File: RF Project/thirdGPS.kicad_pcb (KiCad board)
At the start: 2 copper layers, 30 x 55 mm, 36 parts, among them J1 CONN_Right, J2 CONN_Left, U1 CC2500RGPR, U11 Venus634SMD, U2 U.FL_male, U3 U.FL_male

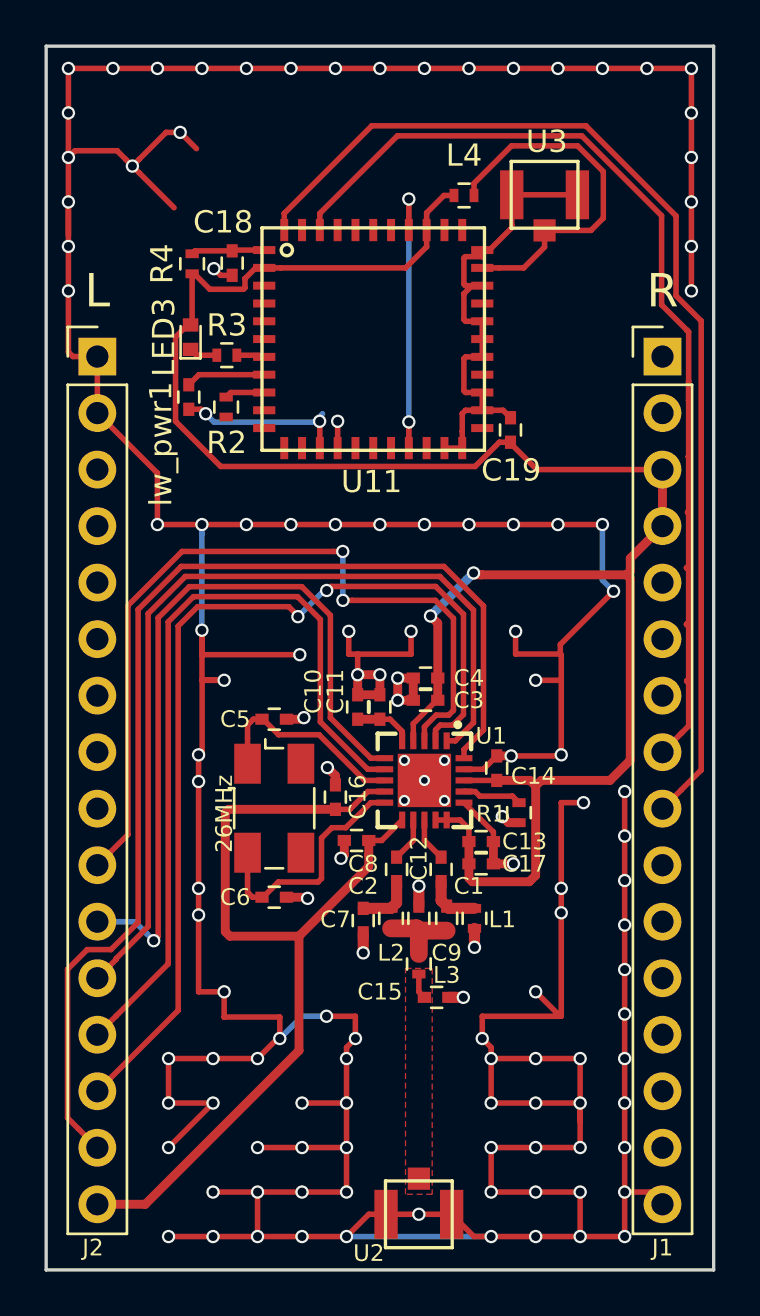
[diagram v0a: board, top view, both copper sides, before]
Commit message: revision component placement, coupling caps added
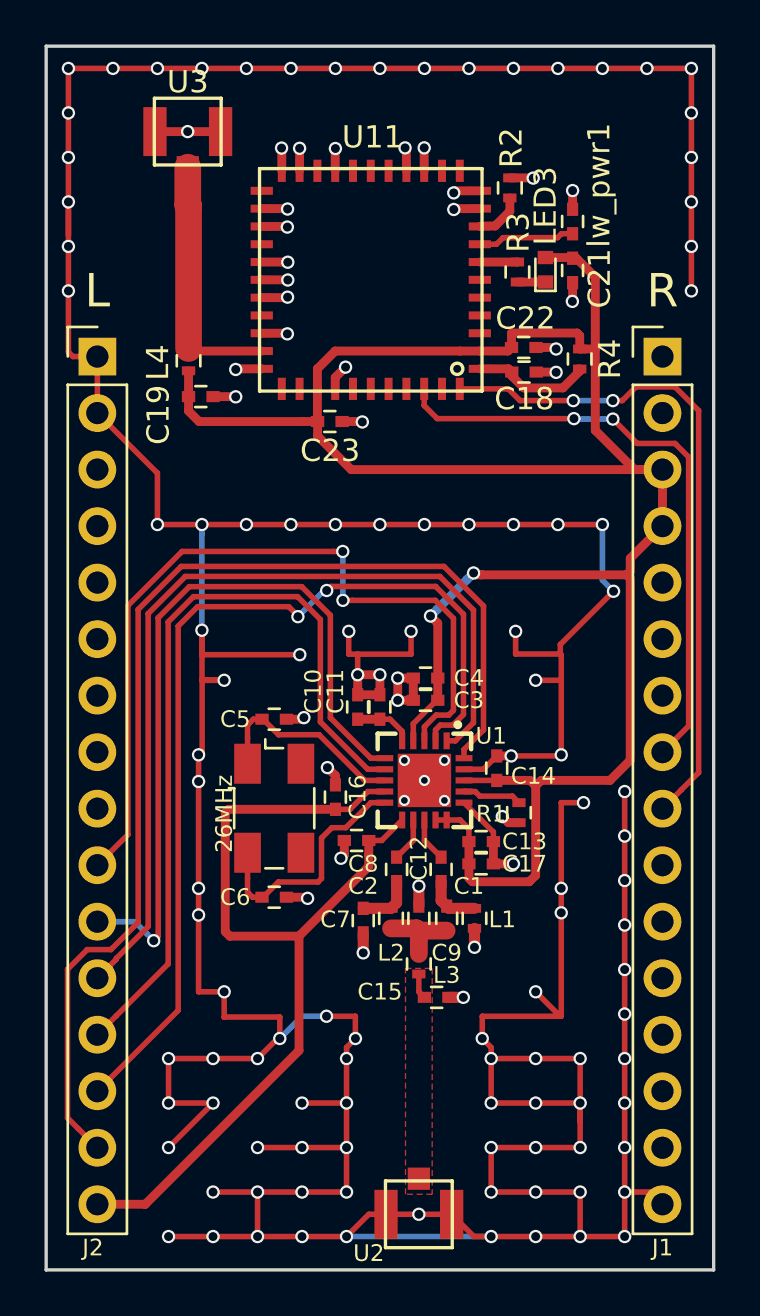
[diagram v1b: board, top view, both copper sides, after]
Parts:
- added C21: 1uF, Capacitors_SMD:C_0402, F.Cu at (108.7, 82.6)
- added C22: 1uF, Capacitors_SMD:C_0402, F.Cu at (106.5, 86.0)
- added C23: 1uF, Capacitors_SMD:C_0402, F.Cu at (97.8, 89.4)
- moved lw_pwr1 19.0 mm to (108.7, 80.4), turned to 90 degrees
- moved R4 17.9 mm to (109.0, 86.6), turned to 270 degrees
- moved U3 16.3 mm to (91.4, 76.3)
- moved LED3 16.2 mm to (107.4, 82.5)
- moved R2 16.1 mm to (105.8, 78.9), turned to 90 degrees
- moved L4 14.4 mm to (91.4, 86.6), turned to 90 degrees
- moved C18 14.0 mm to (106.5, 87.1), turned to 0 degrees
- moved C19 14.0 mm to (92.0, 88.2), turned to 180 degrees
- moved R3 13.6 mm to (106.2, 82.7), turned to 90 degrees
- moved U11 11.1 mm to (104.5, 87.0), turned to 180 degrees
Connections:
- net /GPS/RFIN renamed Net-(L4-Pad2)
- C19 pad 1: RF_GND -> PWR_GND
- U11 pad 21: RF_GND -> PWR_GND
- U11 pad 22: RF_GND -> PWR_GND
- U11 pad 24: RF_GND -> PWR_GND
- U11 pad 25: RF_GND -> PWR_GND
- U11 pad 27: RF_GND -> PWR_GND
- U11 pad 28: RF_GND -> PWR_GND
- U11 pad 29: RF_GND -> PWR_GND
- U11 pad 31: RF_GND -> PWR_GND
- U11 pad 33: RF_GND -> PWR_GND
- U3 pad 1: RF_GND -> PWR_GND
- U3 pad 2: RF_GND -> PWR_GND
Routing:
- net RF_GND: track 22.6 -> 0.00 mm
- net TX: track 49.5 -> 30.2 mm, vias 0 -> 2
- net RX: track 44.5 -> 27.3 mm, vias 0 -> 2
- net AVDD: track 136.1 -> 144.8 mm
- net PWR_GND: track 340.2 -> 333.4 mm, vias 134 -> 149
- net Net-(L4-Pad2): track 16.4 -> 11.5 mm
- net /GPS/RSTN: track 3.31 -> 5.45 mm
- net GPIO24: track 3.58 -> 4.37 mm
